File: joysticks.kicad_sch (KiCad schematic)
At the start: 41 parts, among them J1 DB9_Male_MountingHoles, J2 DB9_Male_MountingHoles

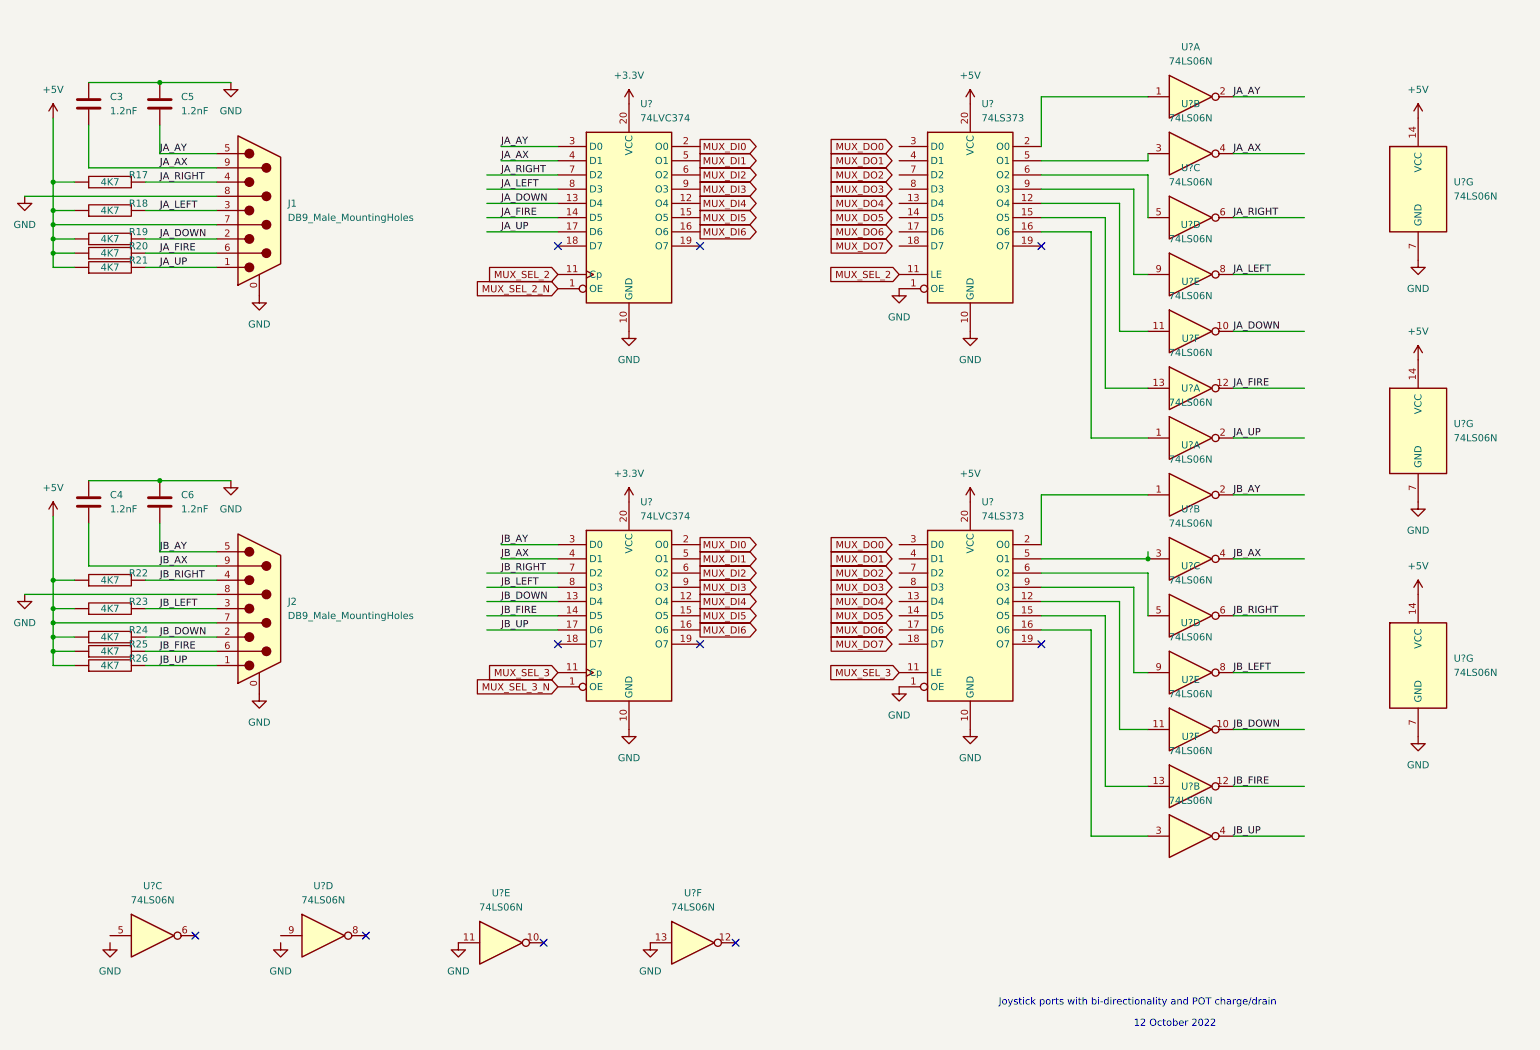
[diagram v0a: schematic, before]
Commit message: add reset button
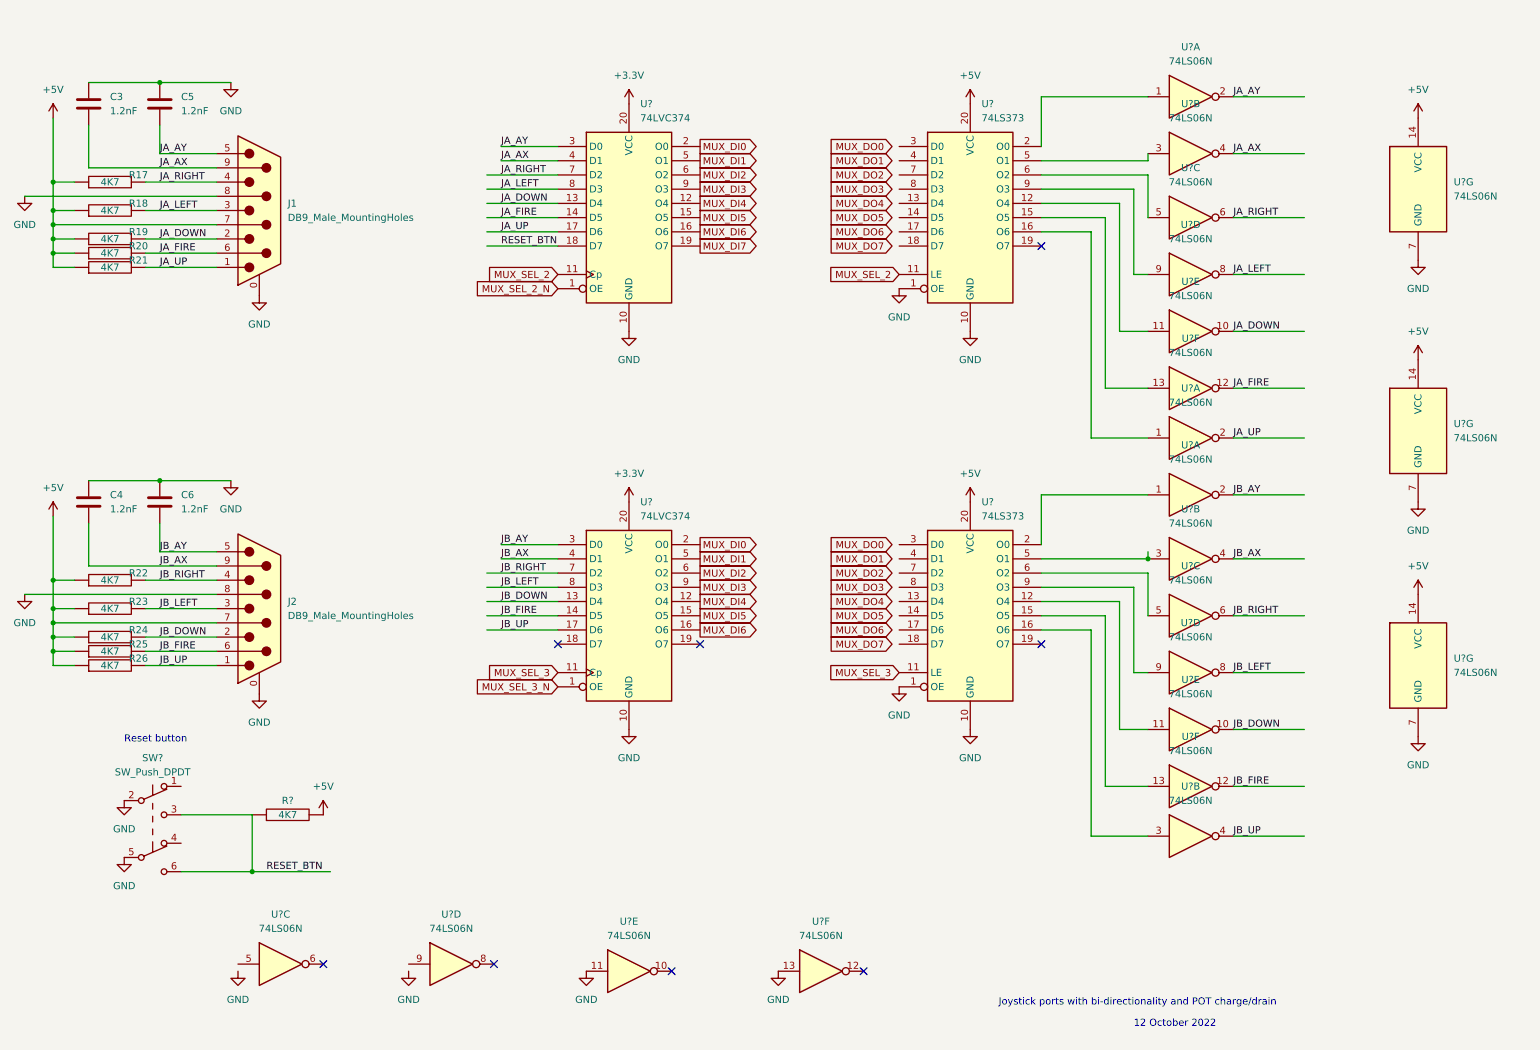
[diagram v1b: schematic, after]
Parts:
- added R?: 4K7, symbol pspice:R
- added SW?: SW_Push_DPDT, snapeda:SPUJ191500, symbol Switch:SW_Push_DPDT
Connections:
- net +5V: now also R?.2
- net GND: now also SW?.2 (B), SW?.5 (B)
- net RESET_BTN: now reaches U?.18 (D7)
- net RESET_BTN: now also R?.1, SW?.3 (C), SW?.6 (C)
- net MUX_DI7: now reaches U?.19 (O7)
- no-connect marks 10 -> 8
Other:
- note added: "Reset button"
- moved on the sheet: U?C, U?D, U?E, U?F

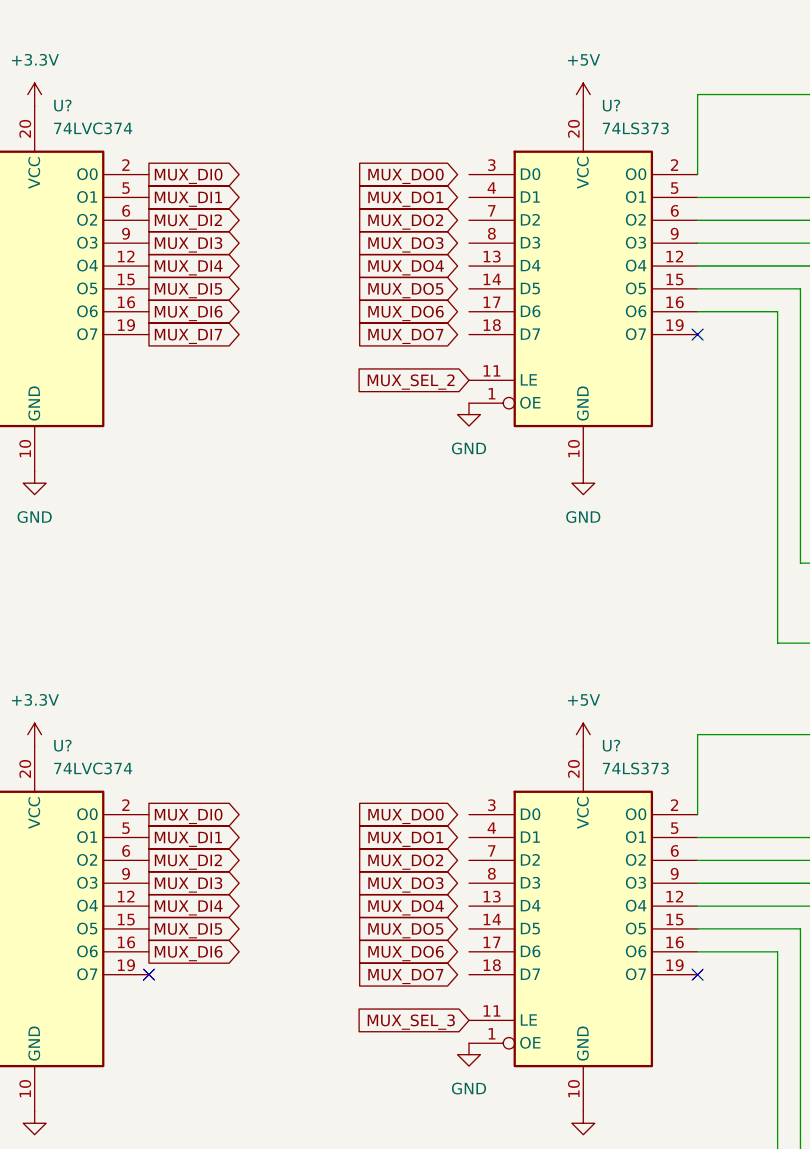
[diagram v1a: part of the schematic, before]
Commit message: begin implementing tape port. add symbols for C64 ports
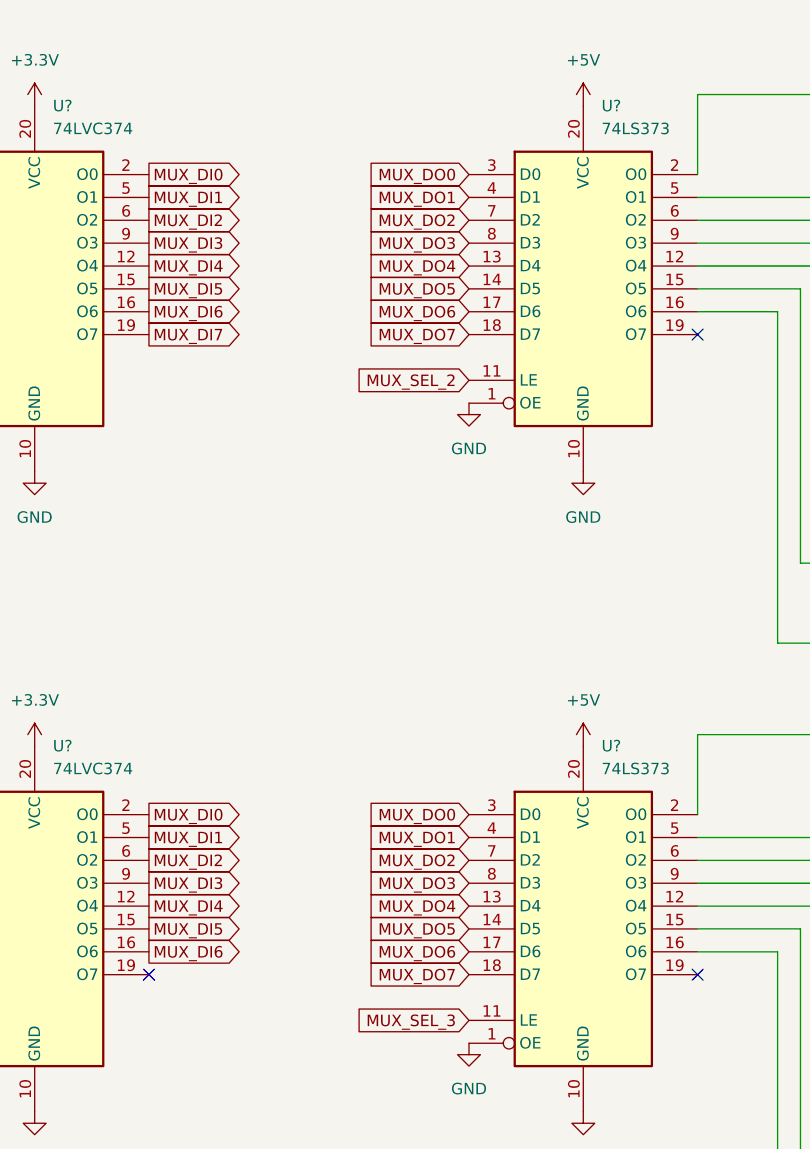
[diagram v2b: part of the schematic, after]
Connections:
- net MUX_DO0: now also U?.3 (D0), U?.3 (D0)
- net MUX_DO1: now also U?.4 (D1), U?.4 (D1)
- net MUX_DO2: now also U?.7 (D2), U?.7 (D2)
- net MUX_DO3: now also U?.8 (D3), U?.8 (D3)
- net MUX_DO4: now also U?.13 (D4), U?.13 (D4)
- net MUX_DO5: now also U?.14 (D5), U?.14 (D5)
- net MUX_DO6: now also U?.17 (D6), U?.17 (D6)
- net MUX_DO7: now also U?.18 (D7), U?.18 (D7)
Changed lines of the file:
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@@
     )
   )
-  (global_label "MUX_DO5" (shape input) (at 170.18 49.53 180) (fields_autoplaced)
+  (global_label "MUX_DO5" (shape input) (at 171.45 49.53 180) (fields_autoplaced)
     (effects (font (size 1.27 1.27)) (justify right))
-    (property "Intersheet References" "${INTERSHEET_REFS}" (id 0) (at 158.9979 49.4506 0)
+    (property "Intersheet References" "${INTERSHEET_REFS}" (id 0) (at 160.2679 49.4506 0)
       (effects (font (size 1.27 1.27)) (justify right) hide)
     )
@@
     )
   )
-  (global_label "MUX_DO7" (shape input) (at 170.18 125.73 180) (fields_autoplaced)
+  (global_label "MUX_DO7" (shape input) (at 171.45 125.73 180) (fields_autoplaced)
     (effects (font (size 1.27 1.27)) (justify right))
-    (property "Intersheet References" "${INTERSHEET_REFS}" (id 0) (at 158.9979 125.6506 0)
+    (property "Intersheet References" "${INTERSHEET_REFS}" (id 0) (at 160.2679 125.6506 0)
       (effects (font (size 1.27 1.27)) (justify right) hide)
     )
   )
-  (global_label "MUX_DO3" (shape input) (at 170.18 115.57 180) (fields_autoplaced)
+  (global_label "MUX_DO3" (shape input) (at 171.45 115.57 180) (fields_autoplaced)
     (effects (font (size 1.27 1.27)) (justify right))
-    (property "Intersheet References" "${INTERSHEET_REFS}" (id 0) (at 158.9979 115.4906 0)
+    (property "Intersheet References" "${INTERSHEET_REFS}" (id 0) (at 160.2679 115.4906 0)
       (effects (font (size 1.27 1.27)) (justify right) hide)
     )
   )
-  (global_label "MUX_DO5" (shape input) (at 170.18 120.65 180) (fields_autoplaced)
+  (global_label "MUX_DO5" (shape input) (at 171.45 120.65 180) (fields_autoplaced)
     (effects (font (size 1.27 1.27)) (justify right))
-    (property "Intersheet References" "${INTERSHEET_REFS}" (id 0) (at 158.9979 120.5706 0)
+    (property "Intersheet References" "${INTERSHEET_REFS}" (id 0) (at 160.2679 120.5706 0)
       (effects (font (size 1.27 1.27)) (justify right) hide)
     )
   )
-  (global_label "MUX_DO4" (shape input) (at 170.18 46.99 180) (fields_autoplaced)
+  (global_label "MUX_DO4" (shape input) (at 171.45 46.99 180) (fields_autoplaced)
     (effects (font (size 1.27 1.27)) (justify right))
-    (property "Intersheet References" "${INTERSHEET_REFS}" (id 0) (at 158.9979 46.9106 0)
+    (property "Intersheet References" "${INTERSHEET_REFS}" (id 0) (at 160.2679 46.9106 0)
       (effects (font (size 1.27 1.27)) (justify right) hide)
     )
@@
     )
   )
-  (global_label "MUX_DO6" (shape input) (at 170.18 52.07 180) (fields_autoplaced)
+  (global_label "MUX_DO6" (shape input) (at 171.45 52.07 180) (fields_autoplaced)
     (effects (font (size 1.27 1.27)) (justify right))
-    (property "Intersheet References" "${INTERSHEET_REFS}" (id 0) (at 158.9979 51.9906 0)
+    (property "Intersheet References" "${INTERSHEET_REFS}" (id 0) (at 160.2679 51.9906 0)
       (effects (font (size 1.27 1.27)) (justify right) hide)
     )
@@
     )
   )
-  (global_label "MUX_DO3" (shape input) (at 170.18 44.45 180) (fields_autoplaced)
+  (global_label "MUX_DO3" (shape input) (at 171.45 44.45 180) (fields_autoplaced)
     (effects (font (size 1.27 1.27)) (justify right))
-    (property "Intersheet References" "${INTERSHEET_REFS}" (id 0) (at 158.9979 44.3706 0)
+    (property "Intersheet References" "${INTERSHEET_REFS}" (id 0) (at 160.2679 44.3706 0)
       (effects (font (size 1.27 1.27)) (justify right) hide)
     )
@@
     )
   )
-  (global_label "MUX_DO1" (shape input) (at 170.18 110.49 180) (fields_autoplaced)
+  (global_label "MUX_DO1" (shape input) (at 171.45 110.49 180) (fields_autoplaced)
     (effects (font (size 1.27 1.27)) (justify right))
-    (property "Intersheet References" "${INTERSHEET_REFS}" (id 0) (at 158.9979 110.4106 0)
+    (property "Intersheet References" "${INTERSHEET_REFS}" (id 0) (at 160.2679 110.4106 0)
       (effects (font (size 1.27 1.27)) (justify right) hide)
     )
@@
     )
   )
-  (global_label "MUX_DO2" (shape input) (at 170.18 41.91 180) (fields_autoplaced)
+  (global_label "MUX_DO2" (shape input) (at 171.45 41.91 180) (fields_autoplaced)
     (effects (font (size 1.27 1.27)) (justify right))
-    (property "Intersheet References" "${INTERSHEET_REFS}" (id 0) (at 158.9979 41.8306 0)
+    (property "Intersheet References" "${INTERSHEET_REFS}" (id 0) (at 160.2679 41.8306 0)
       (effects (font (size 1.27 1.27)) (justify right) hide)
     )
   )
-  (global_label "MUX_DO7" (shape input) (at 170.18 54.61 180) (fields_autoplaced)
+  (global_label "MUX_DO7" (shape input) (at 171.45 54.61 180) (fields_autoplaced)
     (effects (font (size 1.27 1.27)) (justify right))
-    (property "Intersheet References" "${INTERSHEET_REFS}" (id 0) (at 158.9979 54.5306 0)
+    (property "Intersheet References" "${INTERSHEET_REFS}" (id 0) (at 160.2679 54.5306 0)
       (effects (font (size 1.27 1.27)) (justify right) hide)
     )
   )
-  (global_label "MUX_DO6" (shape input) (at 170.18 123.19 180) (fields_autoplaced)
+  (global_label "MUX_DO6" (shape input) (at 171.45 123.19 180) (fields_autoplaced)
     (effects (font (size 1.27 1.27)) (justify right))
-    (property "Intersheet References" "${INTERSHEET_REFS}" (id 0) (at 158.9979 123.1106 0)
+    (property "Intersheet References" "${INTERSHEET_REFS}" (id 0) (at 160.2679 123.1106 0)
       (effects (font (size 1.27 1.27)) (justify right) hide)
     )
@@
     )
   )
-  (global_label "MUX_DO0" (shape input) (at 170.18 107.95 180) (fields_autoplaced)
+  (global_label "MUX_DO0" (shape input) (at 171.45 107.95 180) (fields_autoplaced)
     (effects (font (size 1.27 1.27)) (justify right))
-    (property "Intersheet References" "${INTERSHEET_REFS}" (id 0) (at 158.9979 107.8706 0)
+    (property "Intersheet References" "${INTERSHEET_REFS}" (id 0) (at 160.2679 107.8706 0)
       (effects (font (size 1.27 1.27)) (justify right) hide)
     )
@@
     )
   )
-  (global_label "MUX_DO2" (shape input) (at 170.18 113.03 180) (fields_autoplaced)
+  (global_label "MUX_DO2" (shape input) (at 171.45 113.03 180) (fields_autoplaced)
     (effects (font (size 1.27 1.27)) (justify right))
-    (property "Intersheet References" "${INTERSHEET_REFS}" (id 0) (at 158.9979 112.9506 0)
+    (property "Intersheet References" "${INTERSHEET_REFS}" (id 0) (at 160.2679 112.9506 0)
       (effects (font (size 1.27 1.27)) (justify right) hide)
     )
@@
     )
   )
-  (global_label "MUX_DO0" (shape input) (at 170.18 36.83 180) (fields_autoplaced)
+  (global_label "MUX_DO0" (shape input) (at 171.45 36.83 180) (fields_autoplaced)
     (effects (font (size 1.27 1.27)) (justify right))
-    (property "Intersheet References" "${INTERSHEET_REFS}" (id 0) (at 158.9979 36.7506 0)
+    (property "Intersheet References" "${INTERSHEET_REFS}" (id 0) (at 160.2679 36.7506 0)
       (effects (font (size 1.27 1.27)) (justify right) hide)
     )
@@
     )
   )
-  (global_label "MUX_DO4" (shape input) (at 170.18 118.11 180) (fields_autoplaced)
+  (global_label "MUX_DO4" (shape input) (at 171.45 118.11 180) (fields_autoplaced)
     (effects (font (size 1.27 1.27)) (justify right))
-    (property "Intersheet References" "${INTERSHEET_REFS}" (id 0) (at 158.9979 118.0306 0)
+    (property "Intersheet References" "${INTERSHEET_REFS}" (id 0) (at 160.2679 118.0306 0)
       (effects (font (size 1.27 1.27)) (justify right) hide)
     )
@@
     )
   )
-  (global_label "MUX_DO1" (shape input) (at 170.18 39.37 180) (fields_autoplaced)
+  (global_label "MUX_DO1" (shape input) (at 171.45 39.37 180) (fields_autoplaced)
     (effects (font (size 1.27 1.27)) (justify right))
-    (property "Intersheet References" "${INTERSHEET_REFS}" (id 0) (at 158.9979 39.2906 0)
+    (property "Intersheet References" "${INTERSHEET_REFS}" (id 0) (at 160.2679 39.2906 0)
       (effects (font (size 1.27 1.27)) (justify right) hide)
     )
